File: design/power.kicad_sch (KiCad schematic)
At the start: 5 parts, among them J2 Barrel_Jack, U2 AMS1117-3.3, U3 AMS1117-5.0

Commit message: _
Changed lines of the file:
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@@
+	)
+	(symbol
+		(lib_id "power:VDD")
+		(at 100.33 59.69 0)
+		(unit 1)
+		(exclude_from_sim no)
+		(in_bom yes)
+		(on_board yes)
+		(dnp no)
+		(fields_autoplaced yes)
+		(property "Reference" "#PWR015"
+			(at 100.33 63.5 0)
+			(effects
+				(font
+					(size 1.27 1.27)
+				)
+				(hide yes)
+			)
+		)
+		(property "Value" "+22V_Drive"
+			(at 100.33 54.61 0)
+			(effects
+				(font
+					(size 1.27 1.27)
+				)
+			)
+		)
+		(property "Footprint" ""
+			(at 100.33 59.69 0)
+			(effects
+				(font
+					(size 1.27 1.27)
+				)
+				(hide yes)
+			)
+		)
+		(property "Datasheet" ""
+			(at 100.33 59.69 0)
+			(effects
+				(font
+					(size 1.27 1.27)
+				)
+				(hide yes)
+			)
+		)
+		(property "Description" "Power symbol creates a global label with name \"VDD\""
+			(at 100.33 59.69 0)
+			(effects
+				(font
+					(size 1.27 1.27)
+				)
+				(hide yes)
+			)
+		)
+		(pin "1"
+		)
+		(instances
+			(project "BitCrusher"
+				(path "/e1be550d-9ce6-42b1-a89a-c00b9d7586dd/e3389efa-d643-4121-9f24-b7f22e7fe0ec"
+					(reference "#PWR015")
+					(unit 1)
+				)
+			)
+		)
 	)
 	(symbol
@@
 	)
 	(symbol
-		(lib_id "power:VDD")
-		(at 100.33 59.69 0)
-		(unit 1)
-		(exclude_from_sim no)
-		(in_bom yes)
-		(on_board yes)
-		(dnp no)
-		(fields_autoplaced yes)
-		(property "Reference" "#PWR015"
-			(at 100.33 63.5 0)
-			(effects
-				(font
-					(size 1.27 1.27)
-				)
-				(hide yes)
-			)
-		)
-		(property "Value" "+22V"
-			(at 100.33 54.61 0)
-			(effects
-				(font
-					(size 1.27 1.27)
-				)
-			)
-		)
-		(property "Footprint" ""
-			(at 100.33 59.69 0)
-			(effects
-				(font
-					(size 1.27 1.27)
-				)
-				(hide yes)
-			)
-		)
-		(property "Datasheet" ""
-			(at 100.33 59.69 0)
-			(effects
-				(font
-					(size 1.27 1.27)
-				)
-				(hide yes)
-			)
-		)
-		(property "Description" "Power symbol creates a global label with name \"VDD\""
-			(at 100.33 59.69 0)
-			(effects
-				(font
-					(size 1.27 1.27)
-				)
-				(hide yes)
-			)
-		)
-		(pin "1"
-		)
-		(instances
-			(project ""
-				(path "/e1be550d-9ce6-42b1-a89a-c00b9d7586dd/e3389efa-d643-4121-9f24-b7f22e7fe0ec"
-					(reference "#PWR015")
-					(unit 1)
-				)
-			)
-		)
-	)
-	(symbol
 		(lib_id "power:+5V")
 		(at 96.52 114.3 0)
@@
 					(unit 1)
 				)
+			)
+		)
+	)
+	(symbol
+		(lib_id "power:VDD")
+		(at 114.3 59.69 0)
+		(unit 1)
+		(exclude_from_sim no)
+		(in_bom yes)
+		(on_board yes)
+		(dnp no)
+		(fields_autoplaced yes)
+		(property "Reference" "#PWR04"
+			(at 114.3 63.5 0)
+			(effects
+				(font
+					(size 1.27 1.27)
+				)
+				(hide yes)
+			)
+		)
+		(property "Value" "+22V_Trans"
+			(at 114.3 54.61 0)
+			(effects
+				(font
+					(size 1.27 1.27)
+				)
+			)
+		)
+		(property "Footprint" ""
+			(at 114.3 59.69 0)
+			(effects
+				(font
+					(size 1.27 1.27)
+				)
+				(hide yes)
+			)
+		)
+		(property "Datasheet" ""
+			(at 114.3 59.69 0)
+			(effects
+				(font
+					(size 1.27 1.27)
+				)
+				(hide yes)
+			)
+		)
+		(property "Description" "Power symbol creates a global label with name \"VDD\""
+			(at 114.3 59.69 0)
+			(effects
+				(font
+					(size 1.27 1.27)
+				)
+				(hide yes)
+			)
+		)
+		(pin "1"
+		)
+		(instances
+			(project "BitCrusher"
+				(path "/e1be550d-9ce6-42b1-a89a-c00b9d7586dd/e3389efa-d643-4121-9f24-b7f22e7fe0ec"
+					(reference "#PWR04")
+					(unit 1)
+				)

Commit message: Working on high voltage switching
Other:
- company: UNH Resilient Architecture Lab -> University of New Hampshire, Resilient Architecture Lab
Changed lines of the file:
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@@
 		(title "BitCrusher: Affordable, Open Source EMFI Platform")
 		(rev "0.1")
-		(company "UNH Resilient Architecture Lab")
+		(company "University of New Hampshire, Resilient Architecture Lab")
 		(comment 1 "Advisor: Dean Sullivan")
 		(comment 2 "Author: George Crane")

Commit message: Continuing work on HV switching and primary power distribution
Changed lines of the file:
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@@
 	(text "Should support a peak current of the \nflyback converter I_peak (2A)+10%\n(2.2A)"
 		(exclude_from_sim no)
-		(at 18.034 44.196 0)
+		(at 17.78 44.196 0)
 		(effects
 			(font
@@
 					(unit 1)
 				)
+			)
+		)
+	)
+	(symbol
+		(lib_id "power:VDD")
+		(at 127 59.69 0)
+		(unit 1)
+		(exclude_from_sim no)
+		(in_bom yes)
+		(on_board yes)
+		(dnp no)
+		(fields_autoplaced yes)
+		(property "Reference" "#PWR034"
+			(at 127 63.5 0)
+			(effects
+				(font
+					(size 1.27 1.27)
+				)
+				(hide yes)
+			)
+		)
+		(property "Value" "+6V_Drive"
+			(at 127 54.61 0)
+			(effects
+				(font
+					(size 1.27 1.27)
+				)
+			)
+		)
+		(property "Footprint" ""
+			(at 127 59.69 0)
+			(effects
+				(font
+					(size 1.27 1.27)
+				)
+				(hide yes)
+			)
+		)
+		(property "Datasheet" ""
+			(at 127 59.69 0)
+			(effects
+				(font
+					(size 1.27 1.27)
+				)
+				(hide yes)
+			)
+		)
+		(property "Description" "Power symbol creates a global label with name \"VDD\""
+			(at 127 59.69 0)
+			(effects
+				(font
+					(size 1.27 1.27)
+				)
+				(hide yes)
+			)
+		)
+		(pin "1"
+		)
+		(instances
+			(project "BitCrusher"
+				(path "/e1be550d-9ce6-42b1-a89a-c00b9d7586dd/e3389efa-d643-4121-9f24-b7f22e7fe0ec"
+					(reference "#PWR034")
+					(unit 1)
+				)

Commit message: Working on probe voltage and current sense circuits
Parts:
- renumbered J2 to J6, U2 to U3, U3 to U4

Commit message: Primary power buck regulator
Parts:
- added C30: ${SIM.PARAMS}, Capacitor_SMD:C_1206_3216Metric, symbol Device:C
- added CBOOT1, CFF1, COUT1: 100n, Capacitor_SMD:C_0402_1005Metric, symbol Device:C
- added CHF1: 220n, Capacitor_SMD:C_0805_2012Metric, symbol Device:C
- added CIN1, CIN2: 4.7u, Capacitor_SMD:C_1206_3216Metric, symbol Device:C
- added COUT2, COUT3, COUT4: 22u, Capacitor_SMD:C_1210_3225Metric, symbol Device:C
- added L1: 15.4u, Inductor_SMD:L_TechFuse_SL0630, symbol Device:L
- added RFBB1: 4.76K, Resistor_SMD:R_0402_1005Metric, symbol Device:R
- added RFBT1: 100k, Resistor_SMD:R_0402_1005Metric, symbol Device:R
- added RPG1: ${SIM.PARAMS}, Resistor_SMD:R_0402_1005Metric, symbol Device:R
- added U1: LMR33630ADDA, Package_SO:Texas_HSOP-8-1EP_3.9x4.9mm_P1.27mm_ThermalVias, symbol Regulator_Switching:LMR33630ADDA
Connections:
- net +24V: now also CHF1.1, CIN1.1, CIN2.1, U1.2 (VIN), U1.3 (EN)
- net GND: now also C30.2, CHF1.2, CIN1.2, CIN2.2, COUT1.1, COUT2.1, COUT3.1, COUT4.1, RFBB1.2, U1.1 (GND), U1.9 (GND)
- new net: CFF1.1, RFBB1.1, RFBT1.1, U1.5 (FB)
- new net: CBOOT1.2, L1.1, U1.8 (SW)
- new net: C30.1, RPG1.1, U1.6 (VCC)
- new net: RPG1.2, U1.4 (PG)
- new net: CBOOT1.1, U1.7 (BOOT)
- new net +22V: CFF1.2, COUT1.2, COUT2.2, COUT3.2, COUT4.2, L1.2, RFBT1.2
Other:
- note added: "Capacitor Bank Constraints: Cout_ESR <= 0.0935111400227679 8.54028e-6 <= Cout <= 0.001"

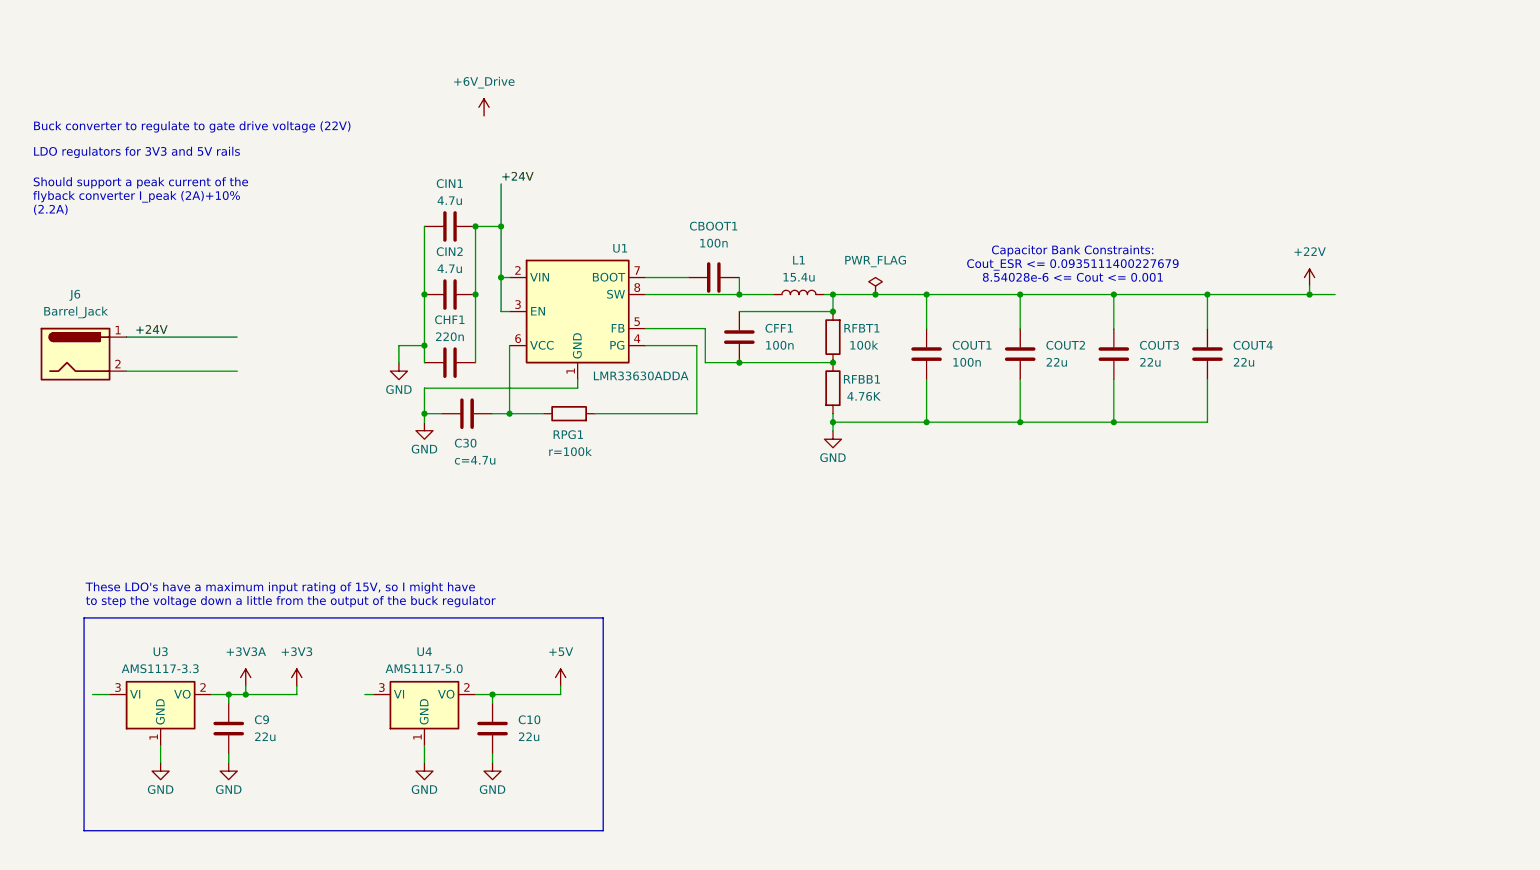
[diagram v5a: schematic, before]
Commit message: Almost finished primary power regulation
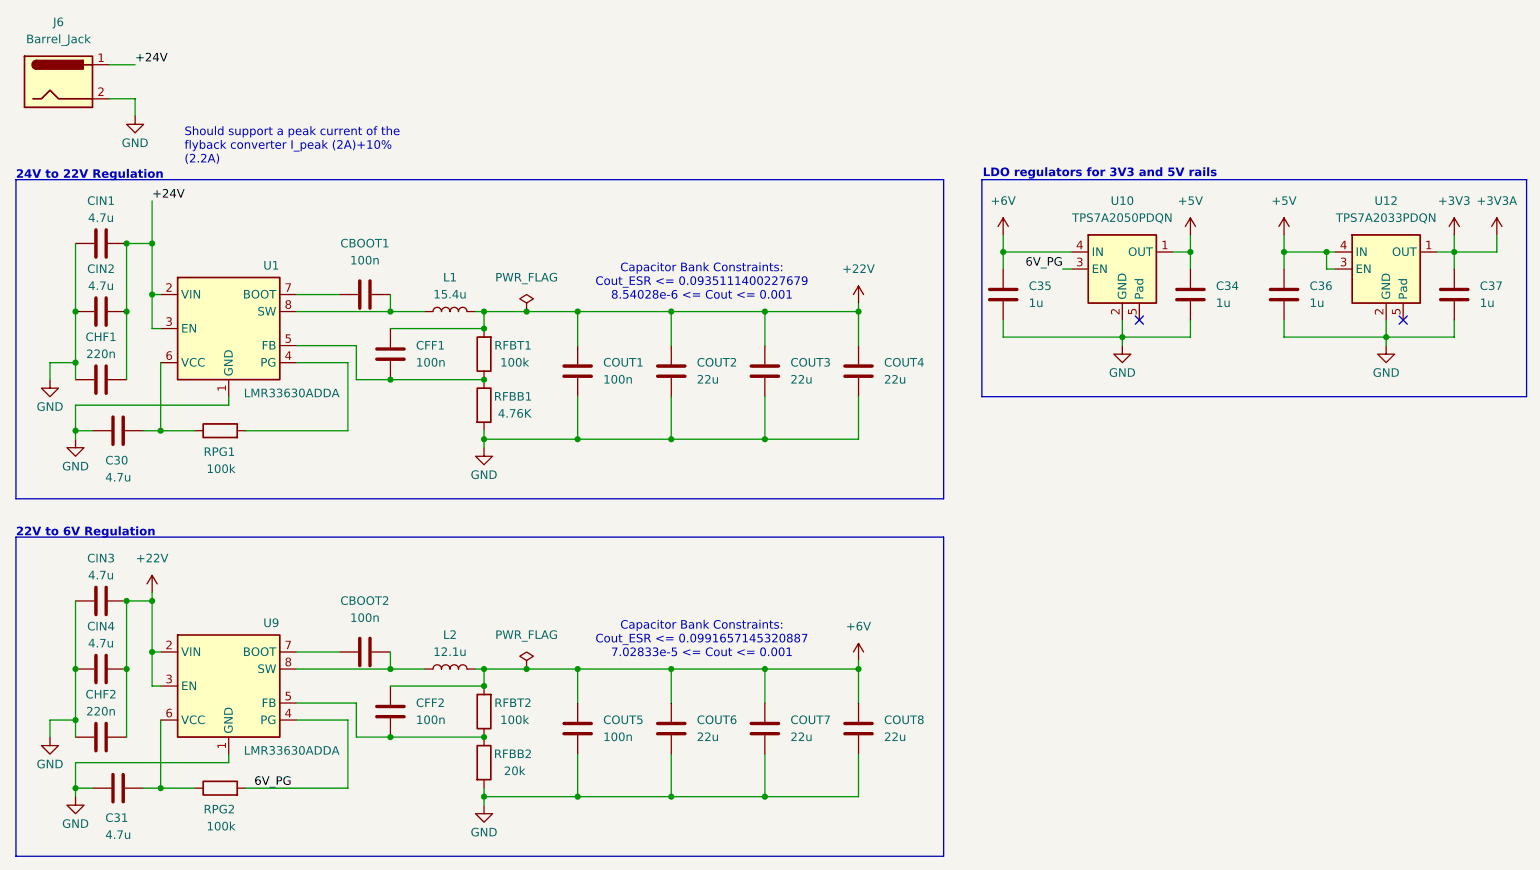
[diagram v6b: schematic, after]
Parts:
- removed C10: 22u, Capacitor_Tantalum_SMD:CP_EIA-3528-21_Kemet-B, symbol Device:C
- removed C9: 22u, symbol Device:C
- removed U3: AMS1117-3.3, Package_TO_SOT_SMD:SOT-223-3_TabPin2, symbol Regulator_Linear:AMS1117-3.3
- removed U4: AMS1117-5.0, Package_TO_SOT_SMD:SOT-223-3_TabPin2, symbol Regulator_Linear:AMS1117-5.0
- added C31, CIN3, CIN4: 4.7u, Capacitor_SMD:C_1206_3216Metric, symbol Device:C
- added C34, C35, C36, C37: 1u, symbol Device:C
- added CBOOT2, CFF2, COUT5: 100n, Capacitor_SMD:C_0402_1005Metric, symbol Device:C
- added CHF2: 220n, Capacitor_SMD:C_0805_2012Metric, symbol Device:C
- added COUT6, COUT7, COUT8: 22u, Capacitor_SMD:C_1210_3225Metric, symbol Device:C
- added L2: 12.1u, Inductor_SMD:L_TechFuse_SL0630, symbol Device:L
- added RFBB2: 20k, Resistor_SMD:R_0402_1005Metric, symbol Device:R
- added RFBT2, RPG2: 100k, Resistor_SMD:R_0402_1005Metric, symbol Device:R
- added U10: TPS7A2050PDQN, Package_SON:Texas_X2SON-4_1x1mm_P0.65mm, symbol Regulator_Linear:TPS7A20xxxDQN
- added U12: TPS7A2033PDQN, Package_SON:Texas_X2SON-4_1x1mm_P0.65mm, symbol Regulator_Linear:TPS7A20xxxDQN
- added U9: LMR33630ADDA, Package_SO:Texas_HSOP-8-1EP_3.9x4.9mm_P1.27mm_ThermalVias, symbol Regulator_Switching:LMR33630ADDA
- C30: value ${SIM.PARAMS} -> 4.7u
- RPG1: value ${SIM.PARAMS} -> 100k
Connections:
- net +22V: now also CHF2.1, CIN3.1, CIN4.1, U9.2 (VIN), U9.3 (EN)
- net +3V3: now also C37.1, U12.1 (OUT)
- net +5V: now also C34.1, C36.1, U10.1 (OUT), U12.3 (EN), U12.4 (IN)
- net GND: now also J6.2, C31.2, C34.2, C35.2, C36.2, C37.2, CHF2.2, CIN3.2, CIN4.2, COUT5.1, COUT6.1, COUT7.1, COUT8.1, RFBB2.2, U10.2 (GND), U12.2 (GND), U9.1 (GND), U9.9 (GND)
- new net: CFF2.1, RFBB2.1, RFBT2.1, U9.5 (FB)
- new net: C31.1, RPG2.1, U9.6 (VCC)
- new net: CBOOT2.1, U9.7 (BOOT)
- new net: CBOOT2.2, L2.1, U9.8 (SW)
- new net +6V: C35.1, CFF2.2, COUT5.2, COUT6.2, COUT7.2, COUT8.2, L2.2, RFBT2.2, U10.4 (IN)
- new net 6V_PG: RPG2.2, U10.3 (EN), U9.4 (PG)
- no-connect marks 0 -> 2
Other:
- note added: "22V to 6V Regulation"
- note added: "24V to 22V Regulation"
- note added: "Capacitor Bank Constraints: Cout_ESR <= 0.0991657145320887 7.02833e-5 <= Cout <= 0.001"
- note removed: "Buck converter to regulate to gate drive voltage (22V)"
- note removed: "These LDO's have a maximum input rating of 15V, so I might have to step the voltage down a little from the output of the buck regulator"
- moved on the sheet: C30, CBOOT1, CFF1, CHF1, CIN1, CIN2, COUT1, COUT2, COUT3, COUT4, J6, L1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

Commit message: Working on measure buffers and assigning footprints
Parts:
- C34, C35, C36, C37: footprint (none) -> Capacitor_SMD:C_0402_1005Metric
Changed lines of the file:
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@@
 			)
 		)
-		(property "Footprint" ""
+		(property "Footprint" "Capacitor_SMD:C_0402_1005Metric"
 			(at 205.4352 59.69 0)
 			(effects
@@
 			)
 		)
-		(property "Footprint" ""
+		(property "Footprint" "Capacitor_SMD:C_0402_1005Metric"
 			(at 163.5252 59.69 0)
 			(effects
@@
 			)
 		)
-		(property "Footprint" ""
+		(property "Footprint" "Capacitor_SMD:C_0402_1005Metric"
 			(at 191.4652 59.69 0)
 			(effects
@@
 			)
 		)
-		(property "Footprint" ""
+		(property "Footprint" "Capacitor_SMD:C_0402_1005Metric"
 			(at 230.8352 59.69 0)
 			(effects
